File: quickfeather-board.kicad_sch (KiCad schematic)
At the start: 101 parts, among them IC1 EOS-S3-QFN, J1 61300211121, J2 1x12_pinhead, J3 1x16_pinhead, J4 S2B-PH-SM4-TB_LF__SN_, J5 0473460001, J6 FTSH-105-01-L-DV-K, J7 61300211121, J8 2x8_pinhead, M1 mounting_pad, M2 mounting_pad, M3 mounting_pad, M4 mounting_pad, Q1 NX3008CBKV, Q2 2N7002PV, Q3 2N7002PV, Q4 DMG1012T-7, U1 TPS62821DLCR, U2 MCP73831T-2ACI_OT, U3 GD25Q16CWIGR, U4 DPS310, U5 MC3635, X1 ECS-_327-12_5-34B-TR

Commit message: [#54927] Standardize supply
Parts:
- C1, C14, C16, C19, C2, C5, C6, C7, D1, N1, Q1, Q4, U1: Author (none) -> Antmicro; License (none) -> Apache-2.0
- C3: Author (none) -> Antmicro; Dielectric (none) -> C0G; License (none) -> Apache-2.0; MPN 0402N101J500CT -> GCM1555C1H101JA16D; Manufacturer WALSIN -> Murata; Voltage (none) -> 50V
- C4: Author (none) -> Antmicro; License (none) -> Apache-2.0; Manufacturer MURATA -> Murata
- D2: footprint quickfeather-board-footprints:LED_0603 -> quicklogic-quickfeather-board-footprints:LED_0603
- D6: Author (none) -> Antmicro; License (none) -> Apache-2.0; Manufacturer Semtec -> Semtech
- IC1: footprint quickfeather-board-footprints:QFN-64_8.5x8.5_EOS -> quicklogic-quickfeather-board-footprints:QFN-64_8.5x8.5_EOS
- J1, J7: footprint quickfeather-board-footprints:PinHeader_1x2_P2.54_Drill0.9mm -> quicklogic-quickfeather-board-footprints:PinHeader_1x2_P2.54_Drill0.9mm
- J2: footprint quickfeather-board-footprints:1x12_pinhead -> quicklogic-quickfeather-board-footprints:1x12_pinhead
- J3: footprint quickfeather-board-footprints:1x16_pinhead -> quicklogic-quickfeather-board-footprints:1x16_pinhead
- J4: footprint quickfeather-board-footprints:PinHeader_2x1mm_P2mm_SMD_RA -> quicklogic-quickfeather-board-footprints:PinHeader_2x1mm_P2mm_SMD_RA
- J5: value 0473460001 -> USB-Micro-B_Molex_473460001
- J6: footprint quickfeather-board-footprints:PinHeader_2x5_P1.27_SMD -> quicklogic-quickfeather-board-footprints:PinHeader_2x5_P1.27_SMD
- J8: footprint quickfeather-board-footprints:2x8_pinhead -> quicklogic-quickfeather-board-footprints:2x8_pinhead
- L1: value DFE201610E-R47M=P2 -> 470n/3.6A; footprint quickfeather-board-footprints:0806 -> antmicro-footprints:L_0806_2016Metric; symbol quickfeather-board:DFE201610E-R47M=P2 -> antmicroFixedInductors:L_470n_3.6A_0806; Author (none) -> Antmicro; Imax (none) -> 3.6A; Isat (none) -> 4.8A; License (none) -> Apache-2.0
- M1, M2, M3, M4: footprint quickfeather-board-footprints:MPAD -> quicklogic-quickfeather-board-footprints:mpad
- N2: footprint quickfeather-board-footprints:LOGO -> quicklogic-quickfeather-board-footprints:LOGO
- R1: Author (none) -> Antmicro; License (none) -> Apache-2.0; MPN MCWR04W1504FTL -> CR0402-FX-1504GLF; Manufacturer Multicomp -> Bourns; Tolerance (none) -> 1%
- R10, R14, R15, R19, R21, R22, R23, R31, R32, R34, R36, R37, R6, R8: Author (none) -> Antmicro; License (none) -> Apache-2.0; MPN CRCW040210K0FKEDHP -> CR0402-FX-1002GLF; Manufacturer VISHAY -> Bourns; Tolerance (none) -> 1%
- R11, R28, R29, R38, R39, R40, R7: Author (none) -> Antmicro; License (none) -> Apache-2.0; MPN CRCW040222R0FKED -> CR0402-FX-22R0GLF; Manufacturer VISHAY -> Bourns; Tolerance (none) -> 1%
- R12, R17, R5: Author (none) -> Antmicro; License (none) -> Apache-2.0; MPN CRCW0402100KFKEDHP -> CR0402-FX-1003GLF; Manufacturer VISHAY -> Bourns; Tolerance (none) -> 1%
- R13, R24, R26: Author (none) -> Antmicro; License (none) -> Apache-2.0; Manufacturer BOURNS -> Bourns; Tolerance (none) -> 1%
- R16: Author (none) -> Antmicro; License (none) -> Apache-2.0; MPN RC0402FR-07200KL -> CR0402-FX-2003GLF; Manufacturer YAGEO_(PHYCOMP) -> Bourns; Tolerance (none) -> 1%
- R18, R2, R20: Author (none) -> Antmicro; License (none) -> Apache-2.0; MPN ERJ2GEJ472X -> CR0402-FX-4701GLF; Manufacturer PANASONIC_ELECTRONIC_COMPONENTS -> Bourns; Tolerance (none) -> 1%
- R25: Author (none) -> Antmicro; License (none) -> Apache-2.0; MPN RMCF0402JT220R -> CR0402-FX-2200GLF; Manufacturer Stackpole Electronics Inc -> Bourns; Tolerance (none) -> 1%
- R27, R3, R9: Author (none) -> Antmicro; License (none) -> Apache-2.0; MPN ERJ2RKF1501X -> CR0402-FX-1501GLF; Manufacturer PANASONIC_ELECTRONIC_COMPONENTS -> Bourns; Tolerance (none) -> 1%
- R30, R33, R41, R42: footprint quickfeather-board-footprints:R_Array_Convex_8x0602 -> quicklogic-quickfeather-board-footprints:R_Array_Convex_8x0602
- R4: Author (none) -> Antmicro; License (none) -> Apache-2.0; MPN CRCW0402453KFKED -> CR0402-FX-4533GLF; Manufacturer VISHAY -> Bourns; Tolerance (none) -> 1%
- S1, S2: value KMR2 -> SW_KMR211NGLFS_SMD
- TP1, TP2, TP6: footprint quickfeather-board-footprints:Testpoint_smd_1mm -> quicklogic-quickfeather-board-footprints:Testpoint_smd_1mm
- TP4, TP5: footprint quickfeather-board-footprints:Testpoint_THT_Drill0.9mm -> quicklogic-quickfeather-board-footprints:Testpoint_THT_Drill0.9mm
- U2: footprint quickfeather-board-footprints:SOT-753 -> quicklogic-quickfeather-board-footprints:SOT-753
- X1: footprint quickfeather-board-footprints:SMD-2_3.2x1.5mm -> quicklogic-quickfeather-board-footprints:SMD-2_3.2x1.5mm
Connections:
- net +3V3: now also C3.2, C4.2; no longer C3.1, C4.1, D6.K, IC1.1 (VCCIOA), IC1.12 (VCCIOB), IC1.24 (VCCIOB), IC1.35 (VCCIOB), IC1.46 (AVDD), IC1.50 (LDO_VIN), IC1.52 (LDO_VIN), IC1.58 (VCCIOA), J1.1, J3.15, J6.1, J7.1, J8.15, R32.1, R34.1, R6.1
- net +VBAT: no longer C2.1, Q1.4 (S2), R12.1
- net +VBUS: now also C1.2, C5.2; no longer C1.1, C5.1
- net ADC0: no longer R16.1, R17.1
- net ADC0_EN: no longer Q1.2 (G1), R37.1
- net ADC1: no longer R28.1
- net GND: now also C1.1, C4.1, C5.1, R5.1; no longer C1.2, C14.2, C16.2, C19.2, C2.2, C4.2, C5.2, C6.2, C7.2, D6.A, Q1.1 (S1), Q4.2 (S), R17.2, R21.2, R22.1, R37.2, R5.2
- net PG: no longer C19.1, Q4.1 (G)
- net PU_CTRL_USBN: no longer R27.1
- net PU_CTRL_USBP: no longer R9.1
- net S3IO_30: no longer R29.1
- net S3IO_32_I2C1: no longer R39.2
- net S3IO_33_I2C1: no longer R40.2
- net S3IO_8: no longer R14.1
- net S3IO_9: no longer R15.1
- net S3_USB_D_N: no longer R7.1
- net S3_USB_D_P: no longer R11.1
- net SPI_MST_CS2: no longer R38.2
- net SPI_SLV_CSn: no longer R21.1, R31.1
- net SPI_SLV_MOSI: no longer R22.2, R23.1
- net SWD_CLK: no longer R32.2
- net SYS_RST: no longer R6.2
- net USB_D_N: no longer R27.2, R7.2
- net USB_D_P: no longer R11.2, R9.2
- net VDD1: no longer C16.1
- net VDD2: no longer C14.1
- net at R4.2, U1.2 (FB): now also C3.1, R5.2; no longer C3.2, R5.1
- net at U2.1 (STAT): no longer R3.2
- net at U2.5 (PROG): no longer R2.1
- net at D2.2: no longer R3.1
- net at IC1.45 (XTAL_O), X1.1: no longer C7.1
- net at IC1.44 (XTAL_I), X1.2: no longer C6.1
- net at R16.2: no longer Q1.3 (D2)
- net at R23.2: no longer J7.2
- net at R31.2: no longer J1.2
- net at J2.2: no longer R38.1
- net at J2.3: no longer R39.1
- net at J2.4: no longer R40.1
- net at J3.10: no longer R29.2
- net at J3.11: no longer R28.2
- net at R2.2: no longer Q4.3 (D)
- new net: IC1.1 (VCCIOA), IC1.12 (VCCIOB), IC1.24 (VCCIOB), IC1.35 (VCCIOB), IC1.46 (AVDD), IC1.50 (LDO_VIN), IC1.52 (LDO_VIN), IC1.58 (VCCIOA)
- new net: J1.1, J7.1
- new net HEADER_3V3: J3.15
- now unconnected: Q1.5 (G2), Q1.6 (D1), R12.2
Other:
- moved on the sheet: C1, C14, C16, C19, C2, C3, C4, C5, C6, C7, D1, D6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

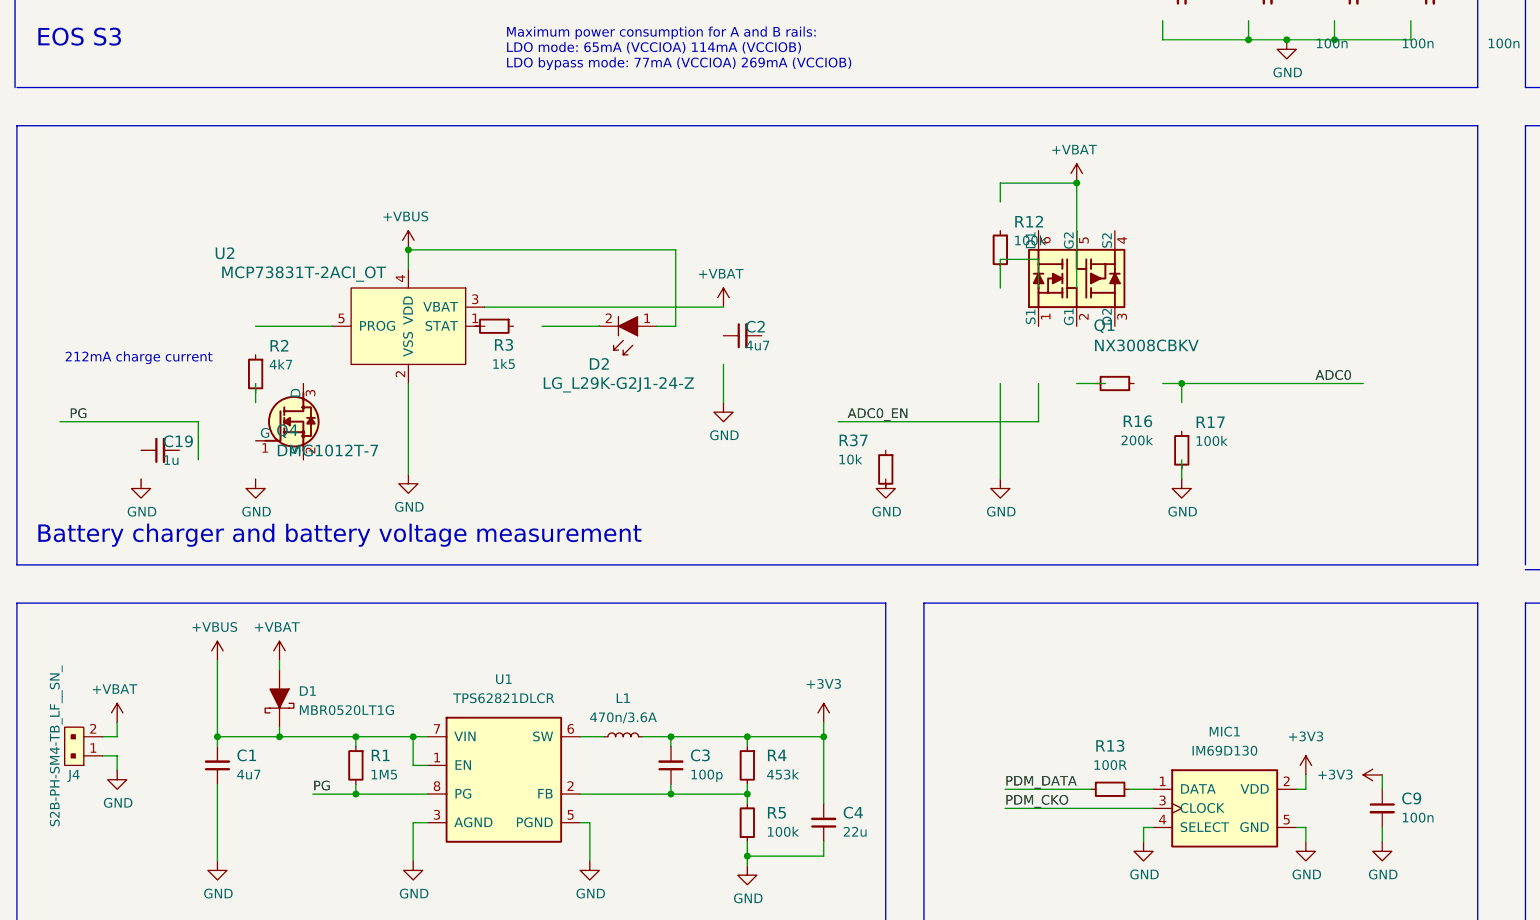
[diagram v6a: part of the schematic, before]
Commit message: [#54927] Standardize battery charger
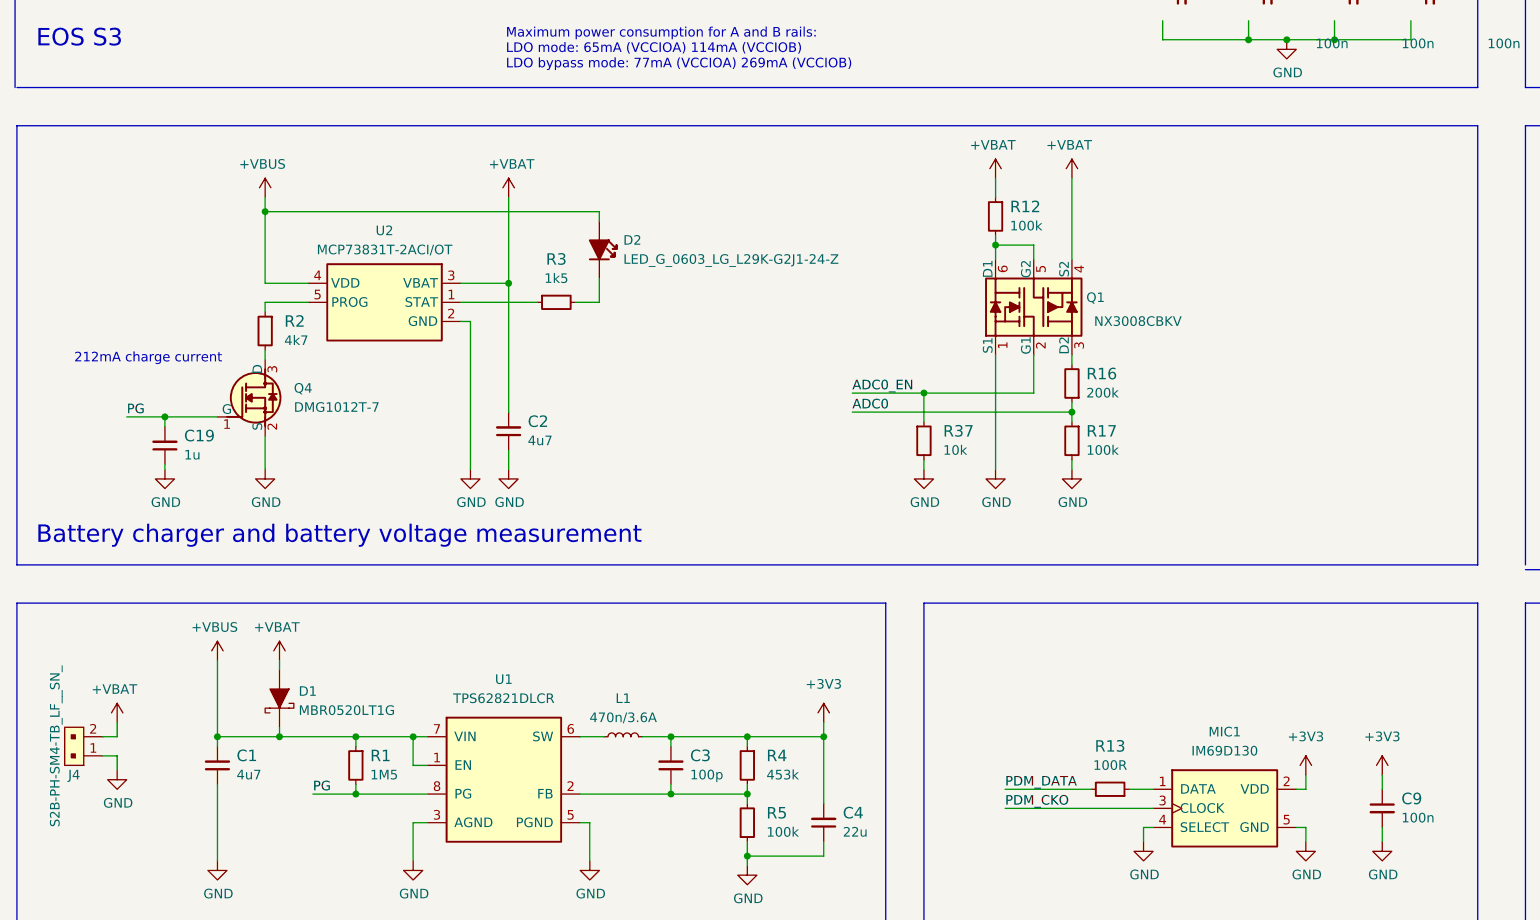
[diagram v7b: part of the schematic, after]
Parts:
- D2: value LG_L29K-G2J1-24-Z -> LED_G_0603_LG_L29K-G2J1-24-Z; footprint quicklogic-quickfeather-board-footprints:LED_0603 -> antmicro-footprints:LED_0603_1608Metric_G; symbol quickfeather-board:LG_L29K-G2J1-24-Z -> antmicroLEDIndicationDiscrete:LED_G_0603_LG_L29K-G2J1-24-Z; Author (none) -> Antmicro; License (none) -> Apache-2.0; Manufacturer OSRAM Opto Semiconductors Inc. -> OSRAM
- U2: value MCP73831T-2ACI_OT -> MCP73831T-2AC_SOT; footprint quicklogic-quickfeather-board-footprints:SOT-753 -> antmicro-footprints:SOT-753; symbol quickfeather-board:MCP73831T-2ACI_OT -> antmicroPMICBatteryChargers:MCP73831T-2AC_SOT; Author (none) -> Antmicro; License (none) -> Apache-2.0
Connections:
- net +VBAT: now also C2.2, Q1.4 (S2), R12.1
- net ADC0: now also R16.1, R17.1
- net ADC0_EN: now also Q1.2 (G1), R37.1
- net GND: now also C19.1, C2.1, Q1.1 (S1), Q4.2 (S), R17.2, R37.2
- net PG: now also C19.2, Q4.1 (G)
- net at U2.1 (STAT): now also R3.1
- net at U2.5 (PROG): now also R2.1
- net at D2.2: now also R3.2
- net at R16.2: now also Q1.3 (D2)
- net at Q1.5 (G2): now also Q1.6 (D1), R12.2
- net at R2.2: now also Q4.3 (D)
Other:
- moved on the sheet: C19, C2, Q1, Q4, R12, R16, R17, R2, R3, R37, U2

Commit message: [#54927] Standardize headers
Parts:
- J2: value 1x12_pinhead -> PinHeader_1x12_P2.54m_Drill1.1mm; footprint quicklogic-quickfeather-board-footprints:1x12_pinhead -> antmicro-footprints:PinHeader_1x12_P2.54_Drill1.1mm; symbol quickfeather-board:1x12_pinhead -> antmicroGenericPinHeaders:PinHeader_1x12_P2.54m_Drill1.1mm; Author (none) -> Antmicro; DNP 1 -> DNP; License (none) -> Apache-2.0; Manufacturer (none) -> Multicomp Pro
- J3: value 1x16_pinhead -> 61301611121; footprint quicklogic-quickfeather-board-footprints:1x16_pinhead -> antmicro-footprints:PinHeader_1x16_P2.54_Drill1.1mm; symbol quickfeather-board:1x16_pinhead -> antmicroGenericPinHeaders:PinHeader_1x16_P2.54mm_Drill1.1mm; Author (none) -> Antmicro; DNP 1 -> DNP; License (none) -> Apache-2.0; MPN 61301611121 -> 61301611121; Manufacturer Wurth Elektronik -> Würth Elektronik
- J6: value FTSH-105-01-L-DV-K -> PinHeader_2x5_P1.27mm_SMD_Latch; footprint quicklogic-quickfeather-board-footprints:PinHeader_2x5_P1.27_SMD -> antmicro-footprints:PinHeader_2x5_P1.27mm_SMD_Latch; symbol quickfeather-board:FTSH-105-01-L-DV-K -> antmicroGenericPinHeaders:PinHeader_2x5_P1.27mm_SMD_Latch; Author (none) -> Antmicro; License (none) -> Apache-2.0; MPN FTSH-105-01-L-DV-K -> FTSH-105-01-F-DV-K; Manufacturer Samtec Inc. -> Samtec
- J8: value 2x8_pinhead -> PinHeader_2x8_P2.54mm_Drill1mm; footprint quicklogic-quickfeather-board-footprints:2x8_pinhead -> antmicro-footprints:PinHeadder_MulticompPro_2213S-16G; symbol quickfeather-board:2x8_pinhead -> antmicroGenericPinHeaders:PinHeader_2x8_P2.54mm_Drill1.1mm; Author (none) -> Antmicro; DNP 1 -> DNP; License (none) -> Apache-2.0; MPN 2213S-16G -> 2213S-16G; Manufacturer Multicomp -> Multicomp Pro
- R21, R22: DNP 1 -> DNP
- R30, R33, R41, R42: value EXB2HV220JV -> 8x22R; footprint quicklogic-quickfeather-board-footprints:R_Array_Convex_8x0602 -> antmicro-footprints:R_Array_8x0602_Panasonic_EXB2HV; symbol quickfeather-board:EXB2HV220JV -> antmicroResistorNetworksArrays:R_8x22R_0602_array; Author (none) -> Antmicro; License (none) -> Apache-2.0; Tolerance (none) -> 5%; Val (none) -> 8x22R
- TP4: value TP_THT -> TP_0.75mm_SMD; footprint quicklogic-quickfeather-board-footprints:Testpoint_THT_Drill0.9mm -> antmicro-footprints:TP_SMD_0.75mm; symbol quickfeather-board:TP_THT -> antmicroTestPoints:TP_0.75mm_SMD; Author (none) -> Antmicro; License (none) -> Apache-2.0; now left out of the parts list
- X1: value ECS-_327-12_5-34B-TR -> Resonator_12MHz_445; footprint quicklogic-quickfeather-board-footprints:SMD-2_3.2x1.5mm -> antmicro-footprints:Resonator_SMD_CTS_445_5x3.2mm; symbol quickfeather-board:ECS-_327-12_5-34B-TR -> antmicroResonators:Resonator_12MHz_445; Author (none) -> Antmicro; License (none) -> Apache-2.0; MPN ECS-.327-12.5-34B-TR -> 445I23D12M00000; Manufacturer ECS Inc. -> CTS; Val (none) -> 12MHz
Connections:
- net HEADER_3V3 is gone; now on net +3V3: J3.15
- net +3V3: now also C12.2, C13.2, C15.2, C17.2, C18.2, D6.K, J1.1, J6.1, J7.1, J8.15, R32.1, R34.1
- net ADC1: now also R28.1
- net GND: now also C12.1, C13.1, C14.1, C15.1, C16.1, C17.1, C18.1, D11.3, D5.3, D6.A, R21.2, R22.1
- net S3IO_30: now also R29.1
- net S3IO_32_I2C1: now also R39.2
- net S3IO_33_I2C1: now also R40.2
- net S3IO_9: now also R15.1
- net SPI_MST_CS2: now also R38.2
- net SPI_SLV_CSn: now also R21.1, R31.1
- net SPI_SLV_MOSI: now also R22.2, R23.1
- net SWD_CLK: now also D5.2 (D-), R32.2
- net SWD_IO: now also D5.1 (D+)
- net SWD_SO: now also D11.1 (D+)
- net SYS_RST: now also D11.2 (D-)
- net VDD1: now also C16.2
- net VDD2: now also C14.2
- net at X1.1: no longer IC1.45 (XTAL_O)
- net at X1.2: no longer IC1.44 (XTAL_I)
- net at R23.2: now also J7.2
- net at R31.2: now also J1.2
- net at J2.2: now also R38.1
- net at J2.3: now also R39.1
- net at J2.4: now also R40.1
- net at J3.10: now also R29.2
- net at J3.11: now also R28.2
- no-connect marks 10 -> 19
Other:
- note removed: "DNP"
- note removed: "const"
- moved on the sheet: C12, C13, C14, C15, C16, C17, C18, D11, D5, D6, J6, J8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
